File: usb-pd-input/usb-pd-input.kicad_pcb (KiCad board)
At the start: 2 copper layers, 2 parts, among them J1 USB_C_Receptacle, U1 CH224K

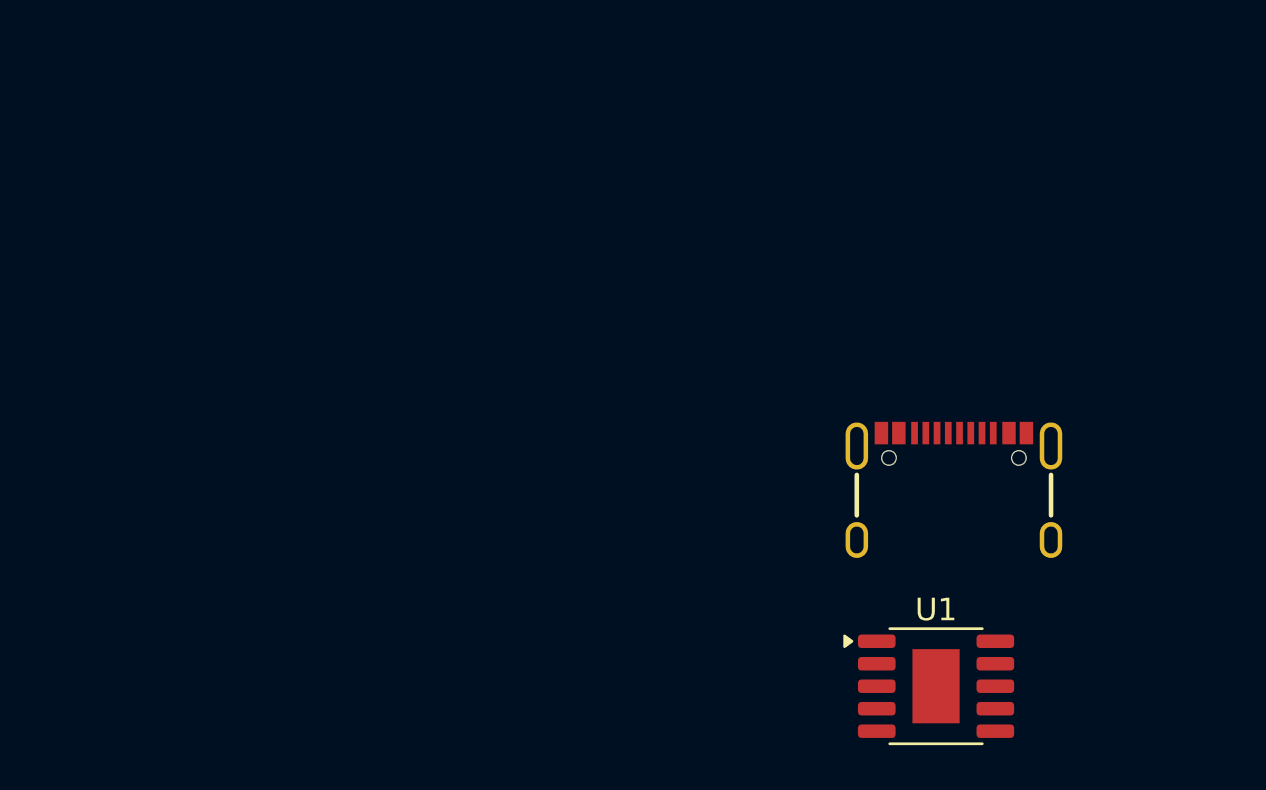
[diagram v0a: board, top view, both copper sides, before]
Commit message: Added USB-PD rough-in
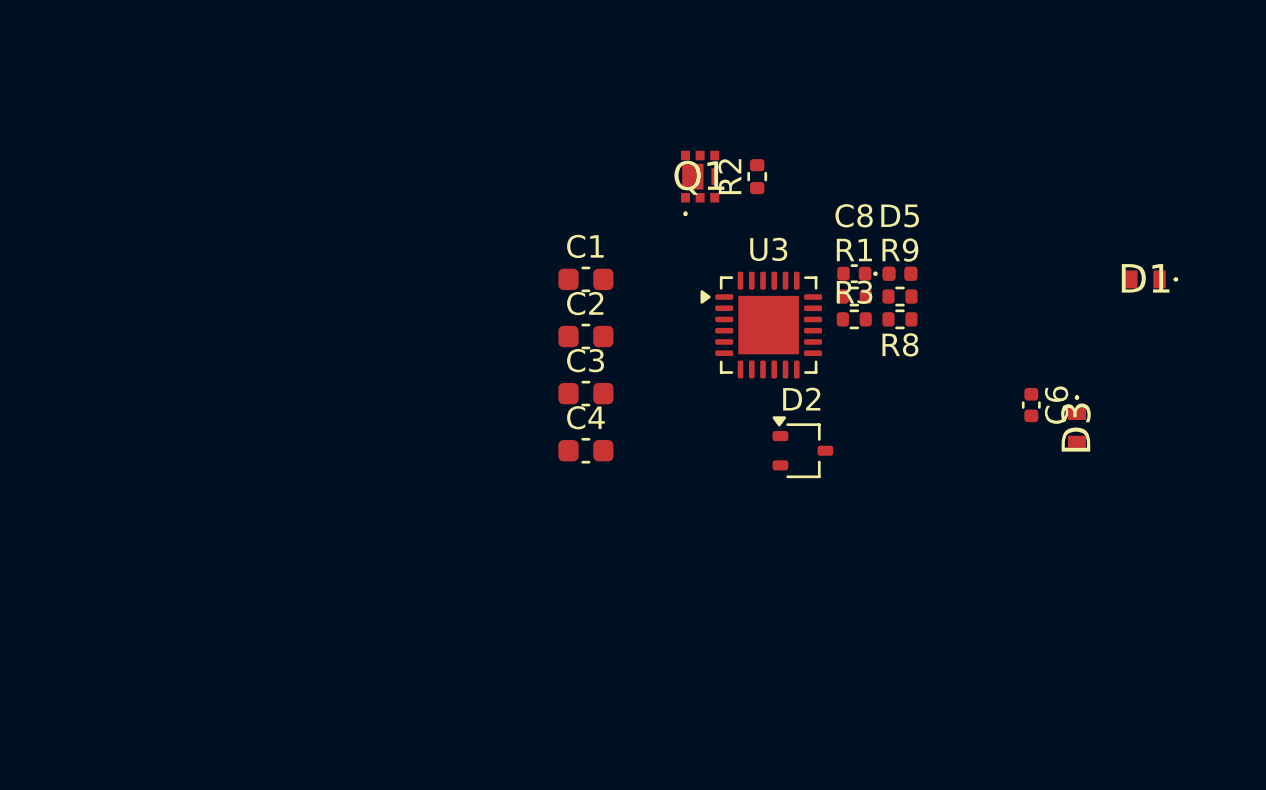
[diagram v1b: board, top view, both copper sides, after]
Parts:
- removed J1: USB_C_Receptacle, PCM_SparkFun-Connector:USB-C_16
- removed U1: CH224K, Package_SO:SSOP-10-1EP_3.9x4.9mm_P1mm_EP2.1x3.3mm
- added C1: 4.7u, Capacitor_SMD:C_0603_1608Metric, F.Cu at (81.8, 57.4)
- added C2: 1u, Capacitor_SMD:C_0603_1608Metric, F.Cu at (81.8, 59.9)
- added C3: 1u, Capacitor_SMD:C_0603_1608Metric, F.Cu at (81.8, 62.5)
- added C4: 1u, Capacitor_SMD:C_0603_1608Metric, F.Cu at (81.8, 65.0)
- added C6: 100n, Capacitor_SMD:C_0402_1005Metric, F.Cu at (101.6, 63.0)
- added C8: 1u, Capacitor_SMD:C_0402_1005Metric, F.Cu at (93.7, 57.1)
- added D1: ESDA25P35, rhinocerose-diodes:ESDA25P351U1M, F.Cu at (106.7, 57.4)
- added D2: ESDA25W, Package_TO_SOT_SMD:SOT-323_SC-70, F.Cu at (91.4, 65.0)
- added D3: ESDA25P35, rhinocerose-diodes:ESDA25P351U1M, F.Cu at (103.6, 64.0)
- added D5: D_Schottky, Diode_SMD:D_0402_1005Metric, F.Cu at (95.8, 57.1)
- added Q1: SSM6J507NU, rhinocerose-transistors:SSM6J507NULF, F.Cu at (86.9, 52.8)
- added R1: 1k, Resistor_SMD:R_0402_1005Metric, F.Cu at (93.7, 58.2)
- added R2: 100k, Resistor_SMD:R_0402_1005Metric, F.Cu at (89.4, 52.8)
- added R3: 18k, Resistor_SMD:R_0402_1005Metric, F.Cu at (93.7, 59.2)
- added R8: 100, Resistor_SMD:R_0402_1005Metric, F.Cu at (95.8, 59.2)
- added R9: 470, Resistor_SMD:R_0402_1005Metric, F.Cu at (95.8, 58.2)
- added U3: STUSB4500, Package_DFN_QFN:QFN-24-1EP_4x4mm_P0.5mm_EP2.7x2.6mm, F.Cu at (89.9, 59.4)

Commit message: Added CH224 schematic
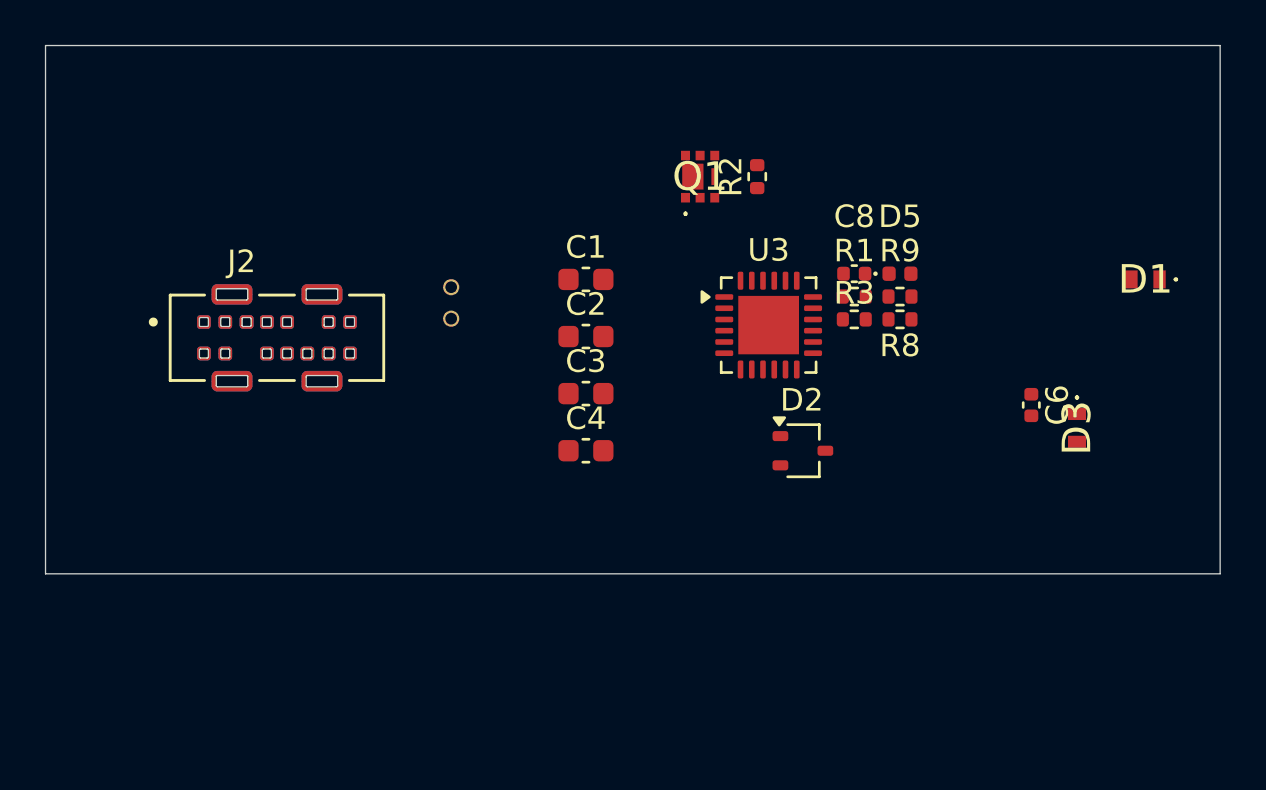
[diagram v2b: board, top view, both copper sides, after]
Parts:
- added J2: 105450-0101, rhinocerose-jacks:CUI_UJ20-C-V-C-2-SMT-TR, F.Cu at (68.0, 60.0)
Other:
- board outline added: 52.2 x 23.5 mm
